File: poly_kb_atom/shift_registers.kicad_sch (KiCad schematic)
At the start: 5 parts, among them U4 74HCT595, U5 74HCT595, U6 74HCT595, U7 74HCT595, U8 74HCT595

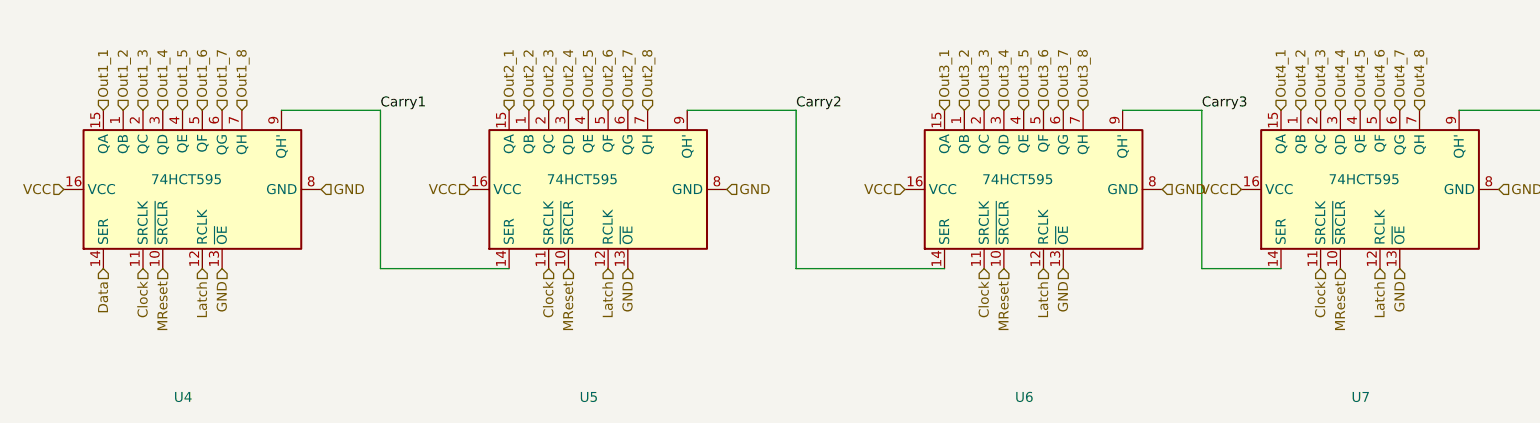
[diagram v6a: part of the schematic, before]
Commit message: QFN shift register version
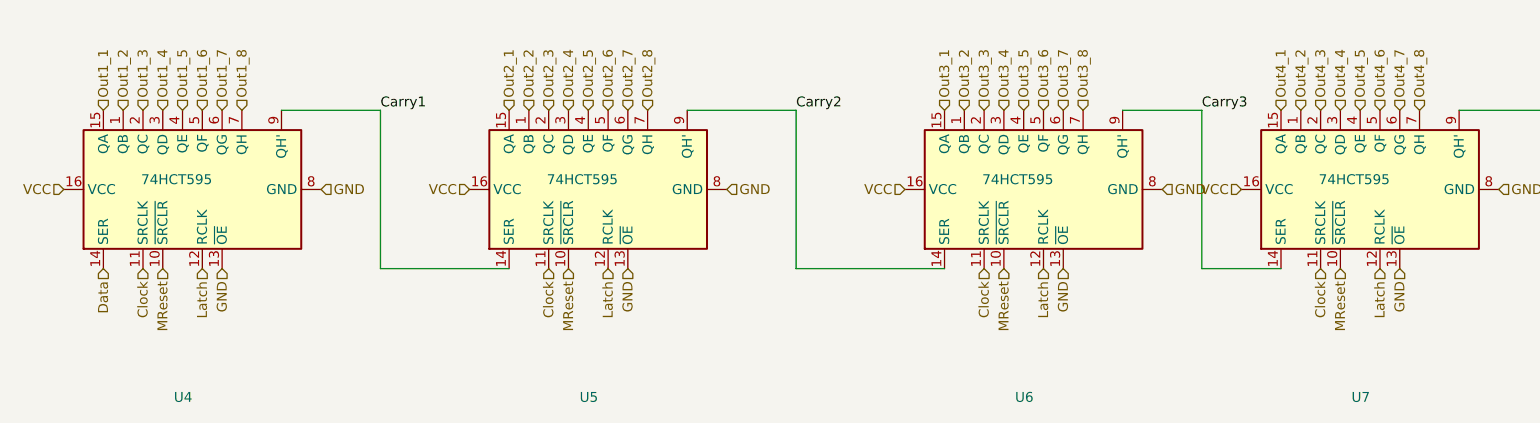
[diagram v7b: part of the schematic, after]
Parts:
- U4, U5, U6, U7, U8: footprint Package_SO:SOIC-16_3.9x9.9mm_P1.27mm -> SOT:SOT-763-1; LCSC C2929943 -> C549185; MPN 74HC595D -> 74HCT595BQ,115
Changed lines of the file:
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@@
     (effects (font (size 1.27 1.27)) (justify left))
   )
-  (symbol (lib_id "74xx:74HCT595") (at 255.27 90.17 90) (unit 1)
+  (symbol (lib_id "74xx:74HCT595") (at 160.02 90.17 90) (unit 1)
     (in_bom yes) (on_board yes)
-    (property "Reference" "U8" (id 0) (at 256.54 116.84 90)
+    (property "Reference" "U6" (id 0) (at 161.29 116.84 90)
       (effects (font (size 1.27 1.27)) (justify left))
     )
-    (property "Value" "74HCT595" (id 1) (at 259.08 88.9 90)
+    (property "Value" "74HCT595" (id 1) (at 163.83 88.9 90)
       (effects (font (size 1.27 1.27)) (justify left))
     )
-    (property "Footprint" "Package_SO:SOIC-16_3.9x9.9mm_P1.27mm" (id 2) (at 255.27 90.17 0)
+    (property "Footprint" "SOT:SOT-763-1" (id 2) (at 160.02 90.17 0)
       (effects (font (size 1.27 1.27)) hide)
     )
-    (property "Datasheet" "https://datasheet.lcsc.com/lcsc/2201121500_Shenzhen-Fuman-Elec-74HC595D-_C2929943.pdf" (id 3) (at 255.27 90.17 0)
+    (property "Datasheet" "https://www.mouser.com/datasheet/2/916/74HC_HCT595-1371408.pdf" (id 3) (at 160.02 90.17 0)
       (effects (font (size 1.27 1.27)) hide)
     )
-    (property "LCSC" "C2929943" (id 4) (at 255.27 90.17 0)
+    (property "LCSC" "C549185" (id 4) (at 160.02 90.17 0)
       (effects (font (size 1.27 1.27)) hide)
     )
-    (property "JLC" "" (id 5) (at 255.27 90.17 0)
-      (effects (font (size 1.27 1.27)) hide)
-    )
-    (property "MPN" "74HC595D" (id 6) (at 255.27 90.17 0)
+    (property "MPN" "74HCT595BQ,115" (id 6) (at 160.02 90.17 0)
       (effects (font (size 1.27 1.27)) hide)
     )
@@
     (pin "9")
   )
-  (symbol (lib_id "74xx:74HCT595") (at 160.02 90.17 90) (unit 1)
+  (symbol (lib_id "74xx:74HCT595") (at 255.27 90.17 90) (unit 1)
     (in_bom yes) (on_board yes)
-    (property "Reference" "U6" (id 0) (at 161.29 116.84 90)
+    (property "Reference" "U8" (id 0) (at 256.54 116.84 90)
       (effects (font (size 1.27 1.27)) (justify left))
     )
-    (property "Value" "74HCT595" (id 1) (at 163.83 88.9 90)
+    (property "Value" "74HCT595" (id 1) (at 259.08 88.9 90)
       (effects (font (size 1.27 1.27)) (justify left))
     )
-    (property "Footprint" "Package_SO:SOIC-16_3.9x9.9mm_P1.27mm" (id 2) (at 160.02 90.17 0)
+    (property "Footprint" "SOT:SOT-763-1" (id 2) (at 255.27 90.17 0)
       (effects (font (size 1.27 1.27)) hide)
     )
-    (property "Datasheet" "https://datasheet.lcsc.com/lcsc/2201121500_Shenzhen-Fuman-Elec-74HC595D-_C2929943.pdf" (id 3) (at 160.02 90.17 0)
+    (property "Datasheet" "https://www.mouser.com/datasheet/2/916/74HC_HCT595-1371408.pdf" (id 3) (at 255.27 90.17 0)
       (effects (font (size 1.27 1.27)) hide)
     )
-    (property "LCSC" "C2929943" (id 4) (at 160.02 90.17 0)
+    (property "LCSC" "C549185" (id 4) (at 255.27 90.17 0)
       (effects (font (size 1.27 1.27)) hide)
     )
-    (property "JLC" "" (id 5) (at 160.02 90.17 0)
+    (property "MPN" "74HCT595BQ,115" (id 6) (at 255.27 90.17 0)
       (effects (font (size 1.27 1.27)) hide)
     )
-    (property "MPN" "74HC595D" (id 6) (at 160.02 90.17 0)
+    (pin "1")
+    (pin "10")
+    (pin "11")
+    (pin "12")
+    (pin "13")
+    (pin "14")
+    (pin "15")
+    (pin "16")
+    (pin "2")
+    (pin "3")
+    (pin "4")
+    (pin "5")
+    (pin "6")
+    (pin "7")
+    (pin "8")
+    (pin "9")
+  )
+  (symbol (lib_id "74xx:74HCT595") (at 203.2 90.17 90) (unit 1)
+    (in_bom yes) (on_board yes)
+    (property "Reference" "U7" (id 0) (at 204.47 116.84 90)
+      (effects (font (size 1.27 1.27)) (justify left))
+    )
+    (property "Value" "74HCT595" (id 1) (at 207.01 88.9 90)
+      (effects (font (size 1.27 1.27)) (justify left))
+    )
+    (property "Footprint" "SOT:SOT-763-1" (id 2) (at 203.2 90.17 0)
+      (effects (font (size 1.27 1.27)) hide)
+    )
+    (property "Datasheet" "https://www.mouser.com/datasheet/2/916/74HC_HCT595-1371408.pdf" (id 3) (at 203.2 90.17 0)
+      (effects (font (size 1.27 1.27)) hide)
+    )
+    (property "LCSC" "C549185" (id 4) (at 203.2 90.17 0)
+      (effects (font (size 1.27 1.27)) hide)
+    )
+    (property "MPN" "74HCT595BQ,115" (id 6) (at 203.2 90.17 0)
       (effects (font (size 1.27 1.27)) hide)
     )
@@
       (effects (font (size 1.27 1.27)) (justify left))
     )
-    (property "Footprint" "Package_SO:SOIC-16_3.9x9.9mm_P1.27mm" (id 2) (at 104.14 90.17 0)
+    (property "Footprint" "SOT:SOT-763-1" (id 2) (at 104.14 90.17 0)
       (effects (font (size 1.27 1.27)) hide)
     )
-    (property "Datasheet" "https://datasheet.lcsc.com/lcsc/2201121500_Shenzhen-Fuman-Elec-74HC595D-_C2929943.pdf" (id 3) (at 104.14 90.17 0)
+    (property "Datasheet" "https://www.mouser.com/datasheet/2/916/74HC_HCT595-1371408.pdf" (id 3) (at 104.14 90.17 0)
       (effects (font (size 1.27 1.27)) hide)
     )
-    (property "LCSC" "C2929943" (id 4) (at 104.14 90.17 0)
+    (property "LCSC" "C549185" (id 4) (at 104.14 90.17 0)
       (effects (font (size 1.27 1.27)) hide)
     )
-    (property "JLC" "" (id 5) (at 104.14 90.17 0)
-      (effects (font (size 1.27 1.27)) hide)
-    )
-    (property "MPN" "74HC595D" (id 6) (at 104.14 90.17 0)
+    (property "MPN" "74HCT595BQ,115" (id 6) (at 104.14 90.17 0)
       (effects (font (size 1.27 1.27)) hide)
     )
@@
       (effects (font (size 1.27 1.27)) (justify left))
     )
-    (property "Value" "74HCT595" (id 1) (at 57.15 88.9 90)
+    (property "Value" "74HCT595" (id 1) (at 55.88 88.9 90)
       (effects (font (size 1.27 1.27)) (justify left))
     )
-    (property "Footprint" "Package_SO:SOIC-16_3.9x9.9mm_P1.27mm" (id 2) (at 52.07 90.17 0)
+    (property "Footprint" "SOT:SOT-763-1" (id 2) (at 52.07 90.17 0)
       (effects (font (size 1.27 1.27)) hide)
     )
-    (property "Datasheet" "https://datasheet.lcsc.com/lcsc/2201121500_Shenzhen-Fuman-Elec-74HC595D-_C2929943.pdf" (id 3) (at 52.07 90.17 0)
+    (property "Datasheet" "https://www.mouser.com/datasheet/2/916/74HC_HCT595-1371408.pdf" (id 3) (at 52.07 90.17 0)
       (effects (font (size 1.27 1.27)) hide)
     )
-    (property "LCSC" "C2929943" (id 4) (at 52.07 90.17 0)
+    (property "LCSC" "C549185" (id 4) (at 52.07 90.17 0)
       (effects (font (size 1.27 1.27)) hide)
     )
-    (property "JLC" "" (id 5) (at 52.07 90.17 0)
+    (property "MPN" "74HCT595BQ,115" (id 6) (at 52.07 90.17 0)
       (effects (font (size 1.27 1.27)) hide)
     )
-    (property "MPN" "74HC595D" (id 6) (at 52.07 90.17 0)
-      (effects (font (size 1.27 1.27)) hide)
-    )
-    (pin "1")
-    (pin "10")
-    (pin "11")
-    (pin "12")
-    (pin "13")
-    (pin "14")
-    (pin "15")
-    (pin "16")
-    (pin "2")
-    (pin "3")
-    (pin "4")
-    (pin "5")
-    (pin "6")
-    (pin "7")
-    (pin "8")
-    (pin "9")
-  )
-  (symbol (lib_id "74xx:74HCT595") (at 203.2 90.17 90) (unit 1)
-    (in_bom yes) (on_board yes)
-    (property "Reference" "U7" (id 0) (at 204.47 116.84 90)
-      (effects (font (size 1.27 1.27)) (justify left))
-    )
-    (property "Value" "74HCT595" (id 1) (at 208.28 88.9 90)
-      (effects (font (size 1.27 1.27)) (justify left))
-    )
-    (property "Footprint" "Package_SO:SOIC-16_3.9x9.9mm_P1.27mm" (id 2) (at 203.2 90.17 0)
-      (effects (font (size 1.27 1.27)) hide)
-    )
-    (property "Datasheet" "https://datasheet.lcsc.com/lcsc/2201121500_Shenzhen-Fuman-Elec-74HC595D-_C2929943.pdf" (id 3) (at 203.2 90.17 0)
-      (effects (font (size 1.27 1.27)) hide)
-    )
-    (property "LCSC" "C2929943" (id 4) (at 203.2 90.17 0)
-      (effects (font (size 1.27 1.27)) hide)
-    )
-    (property "JLC" "" (id 5) (at 203.2 90.17 0)
-      (effects (font (size 1.27 1.27)) hide)
-    )
-    (property "MPN" "74HC595D" (id 6) (at 203.2 90.17 0)
-      (effects (font (size 1.27 1.27)) hide)
-    )

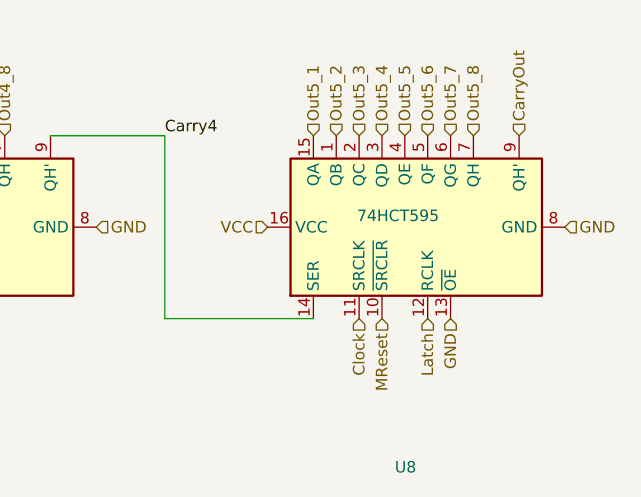
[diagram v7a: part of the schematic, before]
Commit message: Current production version of right side and added STLs
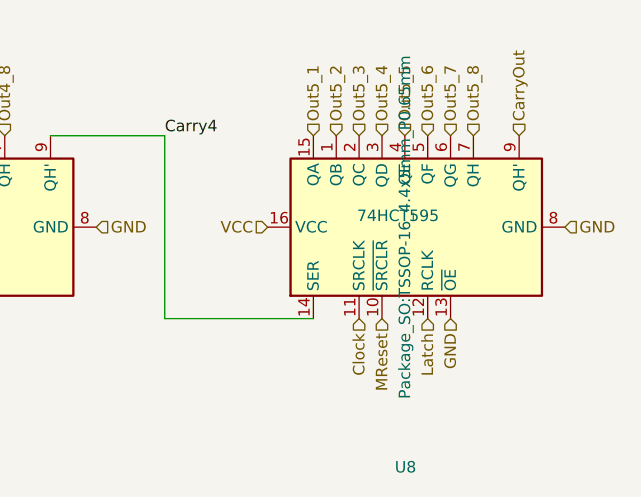
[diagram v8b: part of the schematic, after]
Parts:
- U4, U5, U6, U7, U8: footprint SOT:SOT-763-1 -> Package_SO:TSSOP-16_4.4x5mm_P0.65mm; LCSC C549185 -> (none); MPN 74HCT595BQ,115 -> C152276
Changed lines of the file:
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@@
       (effects (font (size 1.27 1.27)) (justify left))
     )
-    (property "Footprint" "SOT:SOT-763-1" (id 2) (at 160.02 90.17 0)
+    (property "Footprint" "Package_SO:TSSOP-16_4.4x5mm_P0.65mm" (id 2) (at 160.02 90.17 0)
       (effects (font (size 1.27 1.27)) hide)
     )
-    (property "Datasheet" "https://www.mouser.com/datasheet/2/916/74HC_HCT595-1371408.pdf" (id 3) (at 160.02 90.17 0)
+    (property "Datasheet" "https://datasheet.lcsc.com/lcsc/1809171510_onsemi-MC74HCT595ADTR2G_C152276.pdf" (id 3) (at 160.02 90.17 0)
       (effects (font (size 1.27 1.27)) hide)
     )
-    (property "LCSC" "C549185" (id 4) (at 160.02 90.17 0)
+    (property "MPN" "C152276" (id 4) (at 160.02 90.17 0)
       (effects (font (size 1.27 1.27)) hide)
     )
-    (property "MPN" "74HCT595BQ,115" (id 6) (at 160.02 90.17 0)
+    (property "Etc" "" (id 6) (at 160.02 90.17 0)
       (effects (font (size 1.27 1.27)) hide)
     )
@@
       (effects (font (size 1.27 1.27)) (justify left))
     )
-    (property "Footprint" "SOT:SOT-763-1" (id 2) (at 255.27 90.17 0)
+    (property "Footprint" "Package_SO:TSSOP-16_4.4x5mm_P0.65mm" (id 2) (at 255.27 90.17 0))
+    (property "Datasheet" "https://datasheet.lcsc.com/lcsc/1809171510_onsemi-MC74HCT595ADTR2G_C152276.pdf" (id 3) (at 255.27 90.17 0)
       (effects (font (size 1.27 1.27)) hide)
     )
-    (property "Datasheet" "https://www.mouser.com/datasheet/2/916/74HC_HCT595-1371408.pdf" (id 3) (at 255.27 90.17 0)
+    (property "MPN" "C152276" (id 4) (at 255.27 90.17 0)
       (effects (font (size 1.27 1.27)) hide)
     )
-    (property "LCSC" "C549185" (id 4) (at 255.27 90.17 0)
-      (effects (font (size 1.27 1.27)) hide)
-    )
-    (property "MPN" "74HCT595BQ,115" (id 6) (at 255.27 90.17 0)
+    (property "Etc" "" (id 6) (at 255.27 90.17 0)
       (effects (font (size 1.27 1.27)) hide)
     )
@@
       (effects (font (size 1.27 1.27)) (justify left))
     )
-    (property "Footprint" "SOT:SOT-763-1" (id 2) (at 203.2 90.17 0)
+    (property "Footprint" "Package_SO:TSSOP-16_4.4x5mm_P0.65mm" (id 2) (at 203.2 90.17 0)
       (effects (font (size 1.27 1.27)) hide)
     )
-    (property "Datasheet" "https://www.mouser.com/datasheet/2/916/74HC_HCT595-1371408.pdf" (id 3) (at 203.2 90.17 0)
+    (property "Datasheet" "https://datasheet.lcsc.com/lcsc/1809171510_onsemi-MC74HCT595ADTR2G_C152276.pdf" (id 3) (at 203.2 90.17 0)
       (effects (font (size 1.27 1.27)) hide)
     )
-    (property "LCSC" "C549185" (id 4) (at 203.2 90.17 0)
+    (property "MPN" "C152276" (id 4) (at 203.2 90.17 0)
       (effects (font (size 1.27 1.27)) hide)
     )
-    (property "MPN" "74HCT595BQ,115" (id 6) (at 203.2 90.17 0)
+    (property "Etc" "" (id 6) (at 203.2 90.17 0)
       (effects (font (size 1.27 1.27)) hide)
     )
@@
       (effects (font (size 1.27 1.27)) (justify left))
     )
-    (property "Footprint" "SOT:SOT-763-1" (id 2) (at 104.14 90.17 0)
+    (property "Footprint" "Package_SO:TSSOP-16_4.4x5mm_P0.65mm" (id 2) (at 104.14 90.17 0)
       (effects (font (size 1.27 1.27)) hide)
     )
-    (property "Datasheet" "https://www.mouser.com/datasheet/2/916/74HC_HCT595-1371408.pdf" (id 3) (at 104.14 90.17 0)
+    (property "Datasheet" "https://datasheet.lcsc.com/lcsc/1809171510_onsemi-MC74HCT595ADTR2G_C152276.pdf" (id 3) (at 104.14 90.17 0)
       (effects (font (size 1.27 1.27)) hide)
     )
-    (property "LCSC" "C549185" (id 4) (at 104.14 90.17 0)
+    (property "MPN" "C152276" (id 4) (at 104.14 90.17 0)
       (effects (font (size 1.27 1.27)) hide)
     )
-    (property "MPN" "74HCT595BQ,115" (id 6) (at 104.14 90.17 0)
+    (property "Etc" "" (id 6) (at 104.14 90.17 0)
       (effects (font (size 1.27 1.27)) hide)
     )
@@
       (effects (font (size 1.27 1.27)) (justify left))
     )
-    (property "Footprint" "SOT:SOT-763-1" (id 2) (at 52.07 90.17 0)
+    (property "Footprint" "Package_SO:TSSOP-16_4.4x5mm_P0.65mm" (id 2) (at 52.07 90.17 0)
       (effects (font (size 1.27 1.27)) hide)
     )
-    (property "Datasheet" "https://www.mouser.com/datasheet/2/916/74HC_HCT595-1371408.pdf" (id 3) (at 52.07 90.17 0)
+    (property "Datasheet" "https://datasheet.lcsc.com/lcsc/1809171510_onsemi-MC74HCT595ADTR2G_C152276.pdf" (id 3) (at 52.07 90.17 0)
       (effects (font (size 1.27 1.27)) hide)
     )
-    (property "LCSC" "C549185" (id 4) (at 52.07 90.17 0)
+    (property "MPN" "C152276" (id 4) (at 52.07 90.17 0)
       (effects (font (size 1.27 1.27)) hide)
     )
-    (property "MPN" "74HCT595BQ,115" (id 6) (at 52.07 90.17 0)
+    (property "Etc" "" (id 6) (at 52.07 90.17 0)
       (effects (font (size 1.27 1.27)) hide)
     )
